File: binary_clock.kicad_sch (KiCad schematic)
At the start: 30 parts, among them P1 USB_C_Plug_USB2.0, SW1 RESET, SW2 BOOTSEL, U1 RP2040, U2 W25Q32JVSS, U3 AMS1117-3.3, Y1 Crystal_GND23

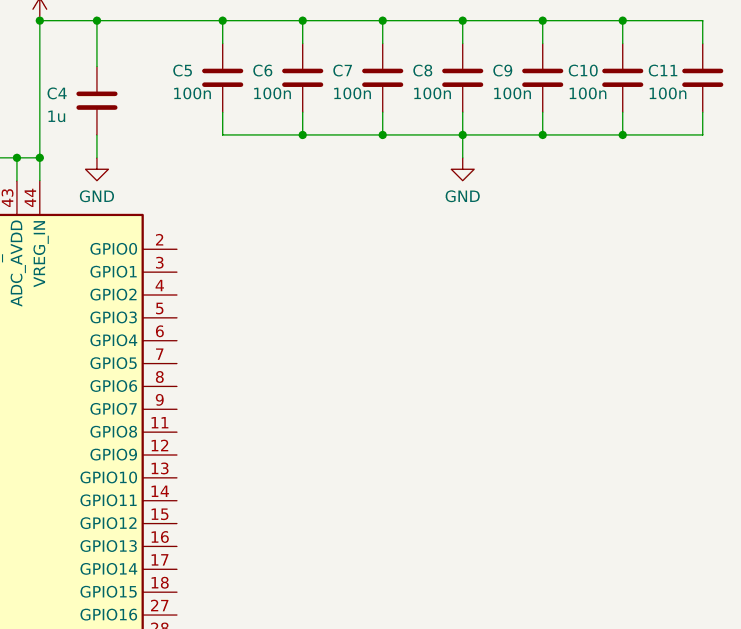
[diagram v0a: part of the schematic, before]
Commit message: added switches and labels for i2c0
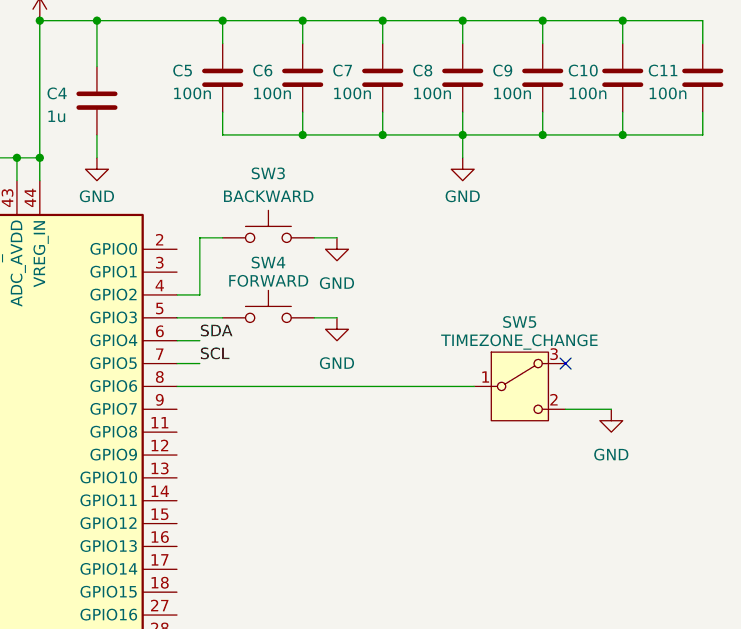
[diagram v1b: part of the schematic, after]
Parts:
- added SW3: BACKWARD, Button_Switch_SMD:SW_SPST_TS-1088-xR020, symbol Switch:SW_Push
- added SW4: FORWARD, Button_Switch_SMD:SW_SPST_TS-1088-xR020, symbol Switch:SW_Push
- added SW5: TIMEZONE_CHANGE, switch:SW_Slide_8.6x3.8x7.0_P2.54mm, symbol Switch:SW_Wuerth_450301014042
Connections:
- net GND: now also SW3.2, SW4.2, SW5.2 (C)
- net at U1.4 (GPIO2): now also SW3.1
- net at U1.5 (GPIO3): now also SW4.1
- net SDA: now reaches U1.6 (GPIO4)
- net SCL: now reaches U1.7 (GPIO5)
- net at U1.8 (GPIO6): now also SW5.1 (B)
- no-connect marks 7 -> 8

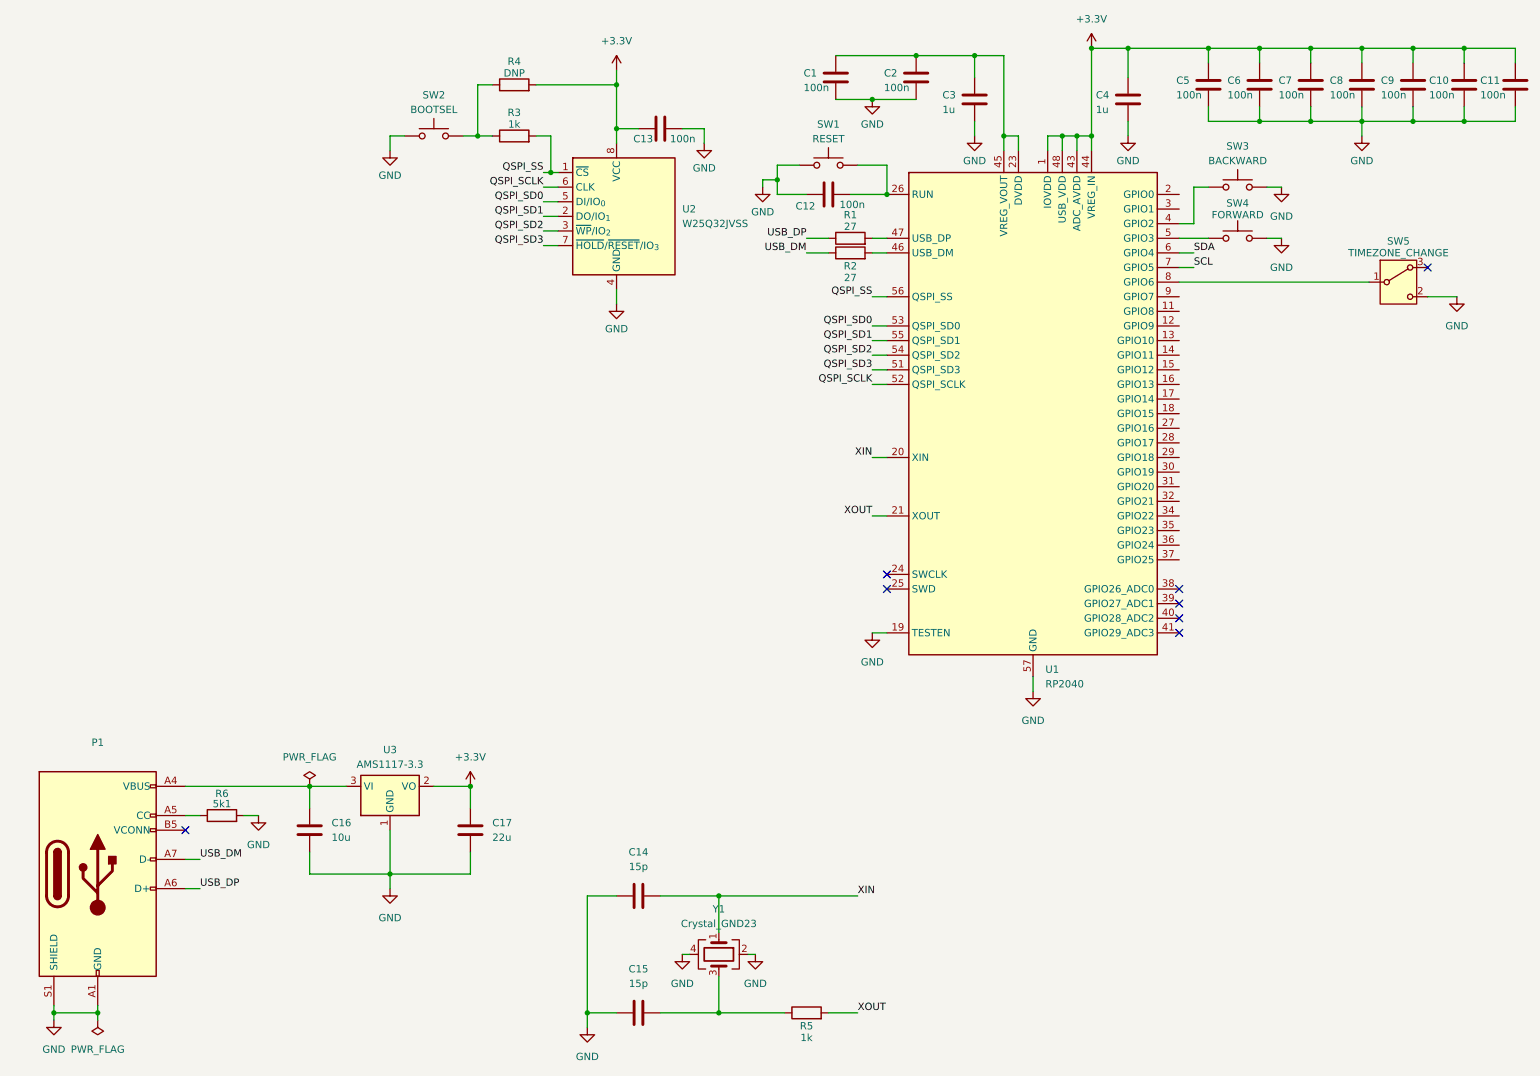
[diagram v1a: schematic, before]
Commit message: added rtc clock and diodes
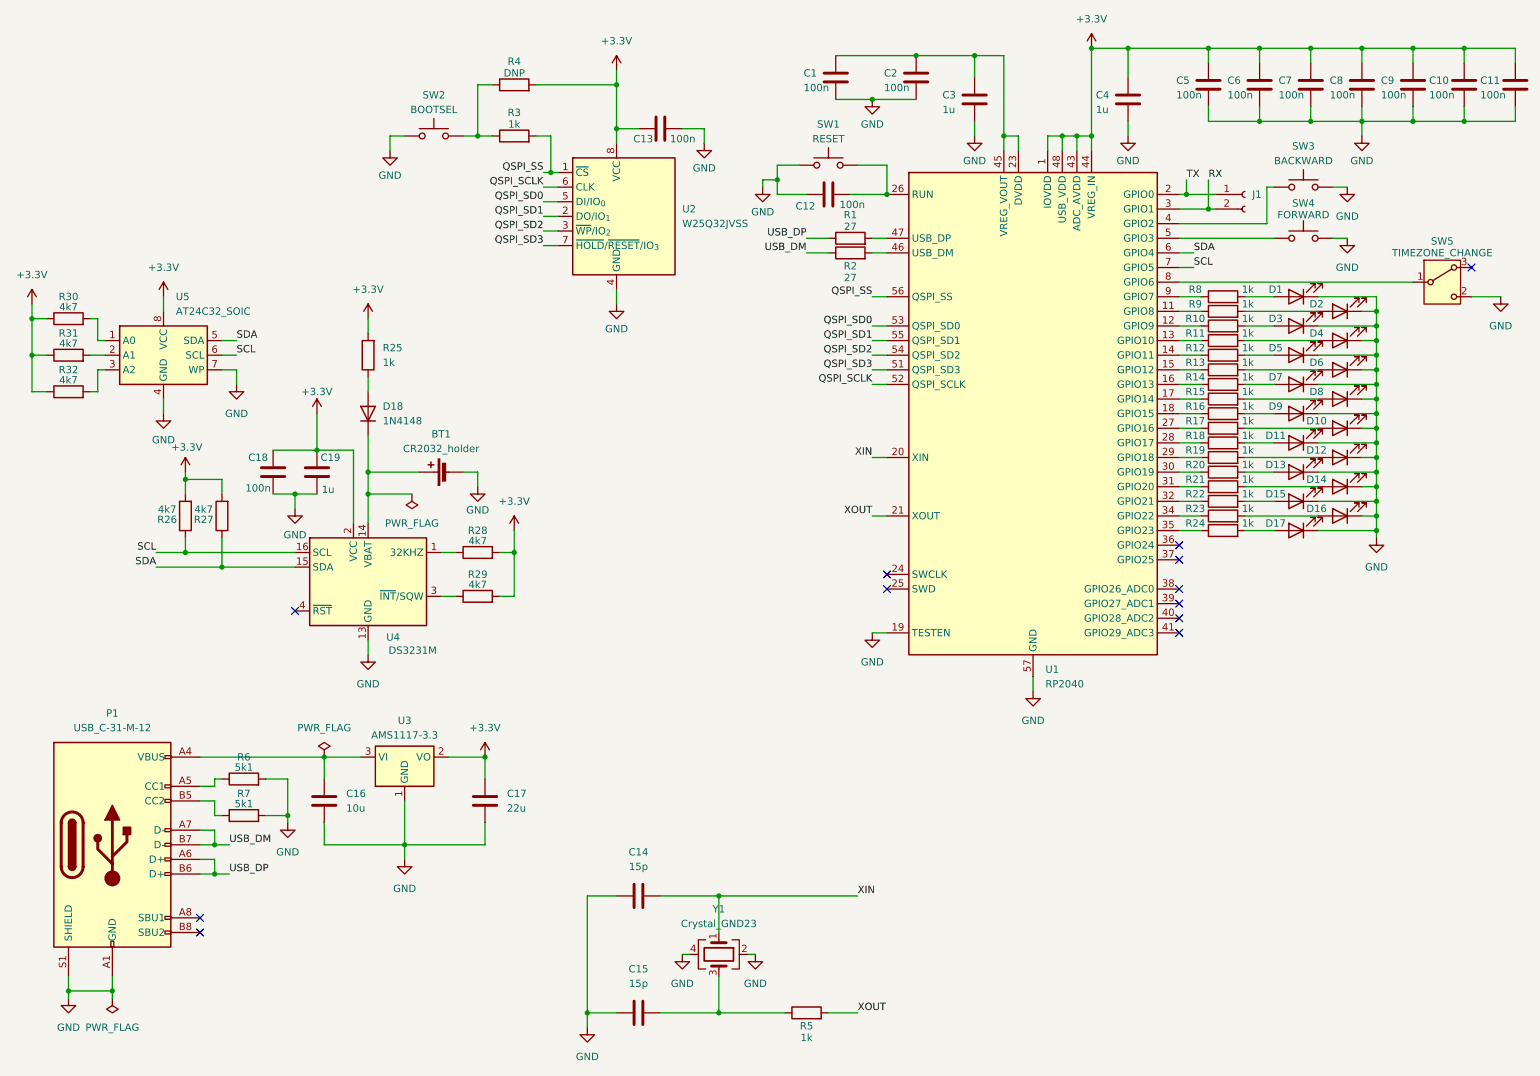
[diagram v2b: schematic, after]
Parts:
- removed P1: USB_C_Plug_USB2.0, Connector_USB:USB_C_Receptacle_GCT_USB4135-GF-A_6P_TopMnt_Horizontal, symbol Connector:USB_C_Plug_USB2.0
- added BT1: CR2032_holder, custom_footprints:Battery_Holder_Coin_2032_BS-7, symbol Device:Battery_Cell
- added C18: 100n, Capacitor_SMD:C_0603_1608Metric, symbol Device:C
- added C19: 1u, Capacitor_SMD:C_0603_1608Metric, symbol Device:C
- added D1, D10, D11, D12, D13, D14, D15, D16, D17, D2, D3, D4, D5, D6, D7, D8, D9: LED, LED_THT:LED_D3.0mm, symbol Device:LED
- added D18: 1N4148, Diode_THT:D_DO-35_SOD27_P7.62mm_Horizontal, symbol Diode:1N4148
- added J1: Conn_01x02_Socket, Connector_PinHeader_2.54mm:PinHeader_1x02_P2.54mm_Vertical, symbol Connector:Conn_01x02_Socket
- added P1: USB_C-31-M-12, Connector_USB:USB_C_Receptacle_HRO_TYPE-C-31-M-12, symbol Connector:USB_C_Receptacle_USB2.0_16P
- added R10, R11, R12, R13, R14, R15, R16, R17, R18, R19, R20, R21, R22, R23, R24, R8, R9: 1k, Resistor_SMD:R_0603_1608Metric, symbol Device:R
- added R25: 1k, Resistor_THT:R_Axial_DIN0207_L6.3mm_D2.5mm_P7.62mm_Horizontal, symbol Device:R
- added R26, R27, R28, R29, R30, R31, R32: 4k7, Resistor_SMD:R_0603_1608Metric, symbol Device:R
- added R7: 5k1, Resistor_SMD:R_0603_1608Metric, symbol Device:R
- added U4: DS3231M, Package_SO:SOIC-16W_7.5x10.3mm_P1.27mm, symbol Timer_RTC:DS3231M
- added U5: AT24C32_SOIC, Package_SO:SOIC-8_3.9x4.9mm_P1.27mm, symbol Memory_EEPROM:AT24CS32-SSHM
- SW5: footprint switch:SW_Slide_8.6x3.8x7.0_P2.54mm -> custom_footprints:SW_Slide_8.6x3.8x7.0_P2.54mm
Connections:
- net +3.3V: now also C18.2, C19.1, R25.2, R26.2, R27.2, R28.2, R29.2, R30.1, R31.1, R32.1, U4.2 (VCC), U5.8 (VCC)
- net GND: now also BT1.2 (-), C18.1, C19.2, D1.1 (K), D10.1 (K), D11.1 (K), D12.1 (K), D13.1 (K), D14.1 (K), D15.1 (K), D16.1 (K), D17.1 (K), D2.1 (K), D3.1 (K), D4.1 (K), D5.1 (K), D6.1 (K), D7.1 (K), D8.1 (K), D9.1 (K), P1.A1 (GND), P1.A12 (GND), P1.B1 (GND), P1.B12 (GND), P1.S1 (SHIELD), R7.2, U4.10 (GND), U4.11 (GND), U4.12 (GND), U4.13 (GND), U4.5 (GND), U4.6 (GND), U4.7 (GND), U4.8 (GND), U4.9 (GND), U5.4 (GND), U5.7 (WP)
- net SCL: now also R26.1, U4.16 (SCL), U5.6 (SCL)
- net SDA: now also R27.1, U4.15 (SDA), U5.5 (SDA)
- net USB_DM: now also P1.A7 (D-), P1.B7 (D-)
- net USB_DP: now also P1.A6 (D+), P1.B6 (D+)
- net at R6.1: now also P1.A5 (CC1)
- net at C16.2, U3.3 (VI): now also P1.A4 (VBUS), P1.A9 (VBUS), P1.B4 (VBUS), P1.B9 (VBUS)
- net at U1.11 (GPIO8): now also R9.1
- net at U1.12 (GPIO9): now also R10.1
- net at U1.13 (GPIO10): now also R11.1
- net at U1.14 (GPIO11): now also R12.1
- net at U1.15 (GPIO12): now also R13.1
- net at U1.16 (GPIO13): now also R14.1
- net at U1.17 (GPIO14): now also R15.1
- net at U1.18 (GPIO15): now also R16.1
- net TX: now reaches U1.2 (GPIO0)
- net TX: now also J1.1 (Pin_1)
- net at U1.27 (GPIO16): now also R17.1
- net at U1.28 (GPIO17): now also R18.1
- net at U1.29 (GPIO18): now also R19.1
- net RX: now reaches U1.3 (GPIO1)
- net RX: now also J1.2 (Pin_2)
- net at U1.30 (GPIO19): now also R20.1
- net at U1.31 (GPIO20): now also R21.1
- net at U1.32 (GPIO21): now also R22.1
- net at U1.34 (GPIO22): now also R23.1
- net at U1.35 (GPIO23): now also R24.1
- net at U1.9 (GPIO7): now also R8.1
- new net: D3.2 (A), R10.2
- new net: D9.2 (A), R16.2
- new net: R28.1, U4.1 (32KHZ)
- new net: BT1.1 (+), D18.1 (K), U4.14 (VBAT)
- new net: R29.1, U4.3 (~{INT}/SQW)
- new net: D18.2 (A), R25.1
- new net: D1.2 (A), R8.2
- new net: D15.2 (A), R22.2
- new net: D2.2 (A), R9.2
- new net: P1.B5 (CC2), R7.1
- new net: D6.2 (A), R13.2
- new net: D14.2 (A), R21.2
- new net: D12.2 (A), R19.2
- new net: D4.2 (A), R11.2
- new net: D17.2 (A), R24.2
- new net: D10.2 (A), R17.2
- new net: D5.2 (A), R12.2
- new net: D11.2 (A), R18.2
- new net: D7.2 (A), R14.2
- new net: D8.2 (A), R15.2
- new net: R31.2, U5.2 (A1)
- new net: R30.2, U5.1 (A0)
- new net: R32.2, U5.3 (A2)
- new net: D13.2 (A), R20.2
- new net: D16.2 (A), R23.2
- no-connect marks 8 -> 12
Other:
- moved on the sheet: C16, C17, SW3, SW4, SW5, U3

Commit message: final pcb, ignore production/
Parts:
- removed J1: Conn_01x02_Socket, Connector_PinHeader_2.54mm:PinHeader_1x02_P2.54mm_Vertical, symbol Connector:Conn_01x02_Socket
- added J1: Conn_01x03_Pin, Connector_PinHeader_2.54mm:PinHeader_1x03_P2.54mm_Vertical, symbol Connector:Conn_01x03_Pin
- P1: value USB_C-31-M-12 -> TYPE-C-31-M-12
- R1, R2: value 27 -> 33
- R4: now not fitted
- SW1: value RESET -> TS-1088-AR02016
- SW2: value BOOTSEL -> TS-1088-AR02016
- SW3: value BACKWARD -> TS-1088-AR02016
- SW4: value FORWARD -> TS-1088-AR02016
- Y1: value Crystal_GND23 -> ABM8-272-T3
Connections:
- net GND: now also J1.3 (Pin_3)
- net RX: now also J1.2 (Pin_2)
- net TX: now also J1.1 (Pin_1)
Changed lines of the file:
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@@
 	)
 	(junction
-		(at 224.79 46.99)
-		(diameter 0)
-		(color 0 0 0 0)
-	)
-	(junction
 		(at 125.73 35.56)
 		(diameter 0)
@@
 	)
 	(junction
-		(at 228.6 49.53)
-		(diameter 0)
-		(color 0 0 0 0)
-	)
-	(junction
 		(at 82.55 95.25)
 		(diameter 0)
@@
 	(wire
 		(pts
+			(xy 271.78 49.53) (xy 275.59 49.53)
+		)
+		(stroke
+			(width 0)
+			(type default)
+		)
+	)
+	(wire
+		(pts
 			(xy 257.81 67.31) (xy 255.27 67.31)
 		)
@@
 	(wire
 		(pts
-			(xy 238.76 45.72) (xy 238.76 52.07)
+			(xy 236.22 45.72) (xy 236.22 52.07)
 		)
 		(stroke
@@
 	(wire
 		(pts
-			(xy 223.52 49.53) (xy 228.6 49.53)
+			(xy 223.52 49.53) (xy 231.14 49.53)
 		)
 		(stroke
@@
 	(wire
 		(pts
+			(xy 271.78 44.45) (xy 275.59 44.45)
+		)
+		(stroke
+			(width 0)
+			(type default)
+		)
+	)
+	(wire
+		(pts
 			(xy 208.28 21.59) (xy 208.28 36.83)
 		)
@@
 	(wire
 		(pts
+			(xy 271.78 46.99) (xy 275.59 46.99)
+		)
+		(stroke
+			(width 0)
+			(type default)
+		)
+	)
+	(wire
+		(pts
 			(xy 281.94 24.13) (xy 281.94 21.59)
 		)
@@
 	(wire
 		(pts
-			(xy 238.76 45.72) (xy 240.03 45.72)
+			(xy 236.22 45.72) (xy 240.03 45.72)
 		)
 		(stroke
@@
 	(wire
 		(pts
-			(xy 223.52 46.99) (xy 224.79 46.99)
+			(xy 223.52 46.99) (xy 231.14 46.99)
 		)
 		(stroke
@@
 	(wire
 		(pts
-			(xy 228.6 49.53) (xy 229.87 49.53)
-		)
-		(stroke
-			(width 0)
-			(type default)
-		)
-	)
-	(wire
-		(pts
 			(xy 59.69 77.47) (xy 57.15 77.47)
 		)
@@
 	(wire
 		(pts
-			(xy 224.79 46.99) (xy 229.87 46.99)
-		)
-		(stroke
-			(width 0)
-			(type default)
-		)
-	)
-	(wire
-		(pts
 			(xy 46.99 64.77) (xy 46.99 67.31)
 		)
@@
 	(wire
 		(pts
-			(xy 228.6 44.45) (xy 228.6 49.53)
-		)
-		(stroke
-			(width 0)
-			(type default)
-		)
-	)
-	(wire
-		(pts
 			(xy 273.05 31.75) (xy 273.05 34.29)
 		)
@@
 	(wire
 		(pts
-			(xy 250.19 45.72) (xy 252.73 45.72)
+			(xy 250.19 45.72) (xy 257.81 45.72)
 		)
 		(stroke
@@
 	(wire
 		(pts
-			(xy 224.79 44.45) (xy 224.79 46.99)
-		)
-		(stroke
-			(width 0)
-			(type default)
-		)
-	)
-	(wire
-		(pts
 			(xy 255.27 102.87) (xy 257.81 102.87)
 		)
@@
 	(wire
 		(pts
-			(xy 223.52 52.07) (xy 238.76 52.07)
+			(xy 223.52 52.07) (xy 236.22 52.07)
 		)
 		(stroke
@@
 	)
 	(label "RX"
-		(at 228.6 44.45 0)
+		(at 231.14 49.53 0)
 		(effects
 			(font
@@
 		)
 	)
+	(label "RX"
+		(at 275.59 46.99 0)
+		(effects
+			(font
+				(size 1.27 1.27)
+			)
+			(justify left bottom)
+		)
+	)
 	(label "QSPI_SS"
 		(at 170.18 64.77 180)
@@
 		)
 	)
+	(label "TX"
+		(at 275.59 44.45 0)
+		(effects
+			(font
+				(size 1.27 1.27)
+			)
+			(justify left bottom)
+		)
+	)
 	(label "XOUT"
 		(at 167.64 189.23 0)
@@
 	)
 	(label "TX"
-		(at 224.79 44.45 0)
+		(at 231.14 46.99 0)
 		(effects
 			(font
@@
 			)
 		)
-		(property "Value" "27"
+		(property "Value" "33"
 			(at 166.37 52.578 90)
 			(effects
@@
 	)
 	(symbol
+		(lib_id "Connector:Conn_01x03_Pin")
+		(at 266.7 46.99 0)
+		(unit 1)
+		(exclude_from_sim no)
+		(in_bom yes)
+		(on_board yes)
+		(dnp no)
+		(fields_autoplaced yes)
+		(property "Reference" "J1"
+			(at 267.335 39.37 0)
+			(effects
+				(font
+					(size 1.27 1.27)
+				)
+			)
+		)
+		(property "Value" "Conn_01x03_Pin"
+			(at 267.335 41.91 0)
+			(effects
+				(font
+					(size 1.27 1.27)
+				)
+			)
+		)
+		(property "Footprint" "Connector_PinHeader_2.54mm:PinHeader_1x03_P2.54mm_Vertical"
+			(at 266.7 46.99 0)
+			(effects
+				(font
+					(size 1.27 1.27)
+				)
+				(hide yes)
+			)
+		)
+		(property "Datasheet" "~"
+			(at 266.7 46.99 0)
+			(effects
+				(font
+					(size 1.27 1.27)
+				)
+				(hide yes)
+			)
+		)
+		(property "Description" "Generic connector, single row, 01x03, script generated"
+			(at 266.7 46.99 0)
+			(effects
+				(font
+					(size 1.27 1.27)
+				)
+				(hide yes)
+			)
+		)
+		(pin "1"
+		)
+		(pin "3"
+		)
+		(pin "2"
+		)
+		(instances
+			(project "binary_clock"
+				(path "/e502a73f-a3d5-4755-8e23-06b2a601e58a"
+					(reference "J1")
+					(unit 1)
+				)
+			)
+		)
+	)
+	(symbol
 		(lib_id "power:GND")
 		(at 86.36 39.37 0)
@@
 		(in_bom yes)
 		(on_board yes)
-		(dnp no)
+		(dnp yes)
 		(property "Reference" "R4"
 			(at 107.95 23.876 90)
@@
 			)
 		)
-		(property "Value" "RESET"
+		(property "Value" "TS-1088-AR02016"
 			(at 162.56 37.338 0)
 			(effects
@@
 			)
 		)
-		(property "Value" "USB_C-31-M-12"
+		(property "Value" "TYPE-C-31-M-12"
 			(at 38.1 139.7 0)
 			(effects
@@
 	)
 	(symbol
-		(lib_id "Connector:Conn_01x02_Socket")
-		(at 234.95 46.99 0)
+		(lib_id "power:GND")
+		(at 275.59 49.53 0)
 		(unit 1)
 		(exclude_from_sim no)
@@
 		(on_board yes)
 		(dnp no)
-		(fields_autoplaced yes)
-		(property "Reference" "J1"
-			(at 236.22 46.9899 0)
+		(property "Reference" "#PWR035"
+			(at 275.59 55.88 0)
 			(effects
 				(font
 					(size 1.27 1.27)
 				)
-				(justify left)
+				(hide yes)
 			)
 		)
-		(property "Value" "Conn_01x02_Socket"
-			(at 236.22 49.5299 0)
+		(property "Value" "GND"
+			(at 275.59 53.848 0)
 			(effects
 				(font
 					(size 1.27 1.27)
 				)
-				(justify left)
-				(hide yes)
 			)
 		)
-		(property "Footprint" "Connector_PinHeader_2.54mm:PinHeader_1x02_P2.54mm_Vertical"
-			(at 234.95 46.99 0)
+		(property "Footprint" ""
+			(at 275.59 49.53 0)
 			(effects
 				(font
@@
 			)
 		)
-		(property "Datasheet" "~"
-			(at 234.95 46.99 0)
+		(property "Datasheet" ""
+			(at 275.59 49.53 0)
 			(effects
 				(font
@@
 			)
 		)
-		(property "Description" "Generic connector, single row, 01x02, script generated"
-			(at 234.95 46.99 0)
+		(property "Description" "Power symbol creates a global label with name \"GND\" , ground"
+			(at 275.59 49.53 0)
 			(effects
 				(font
@@
 			)
 		)
-		(pin "2"
-		)
 		(pin "1"
 		)
 		(instances
-			(project ""
+			(project "binary_clock"
 				(path "/e502a73f-a3d5-4755-8e23-06b2a601e58a"
-					(reference "J1")
+					(reference "#PWR035")
 					(unit 1)
 				)
@@
 			)
 		)
-		(property "Value" "BACKWARD"
-			(at 245.11 41.148 0)
+		(property "Value" "TS-1088-AR02016"
+			(at 243.586 41.148 0)
 			(effects
 				(font
@@
 			)
 		)
-		(property "Value" "FORWARD"
-			(at 245.11 50.546 0)
+		(property "Value" "TS-1088-AR02016"
+			(at 245.872 50.292 0)
 			(effects
 				(font
@@
 			)
 		)
-		(property "Value" "BOOTSEL"
+		(property "Value" "TS-1088-AR02016"
 			(at 93.98 32.258 0)
 			(effects
@@
 	(symbol
 		(lib_id "power:GND")
-		(at 252.73 45.72 0)
+		(at 257.81 45.72 0)
 		(unit 1)
 		(exclude_from_sim no)
@@
 		(fields_autoplaced yes)
 		(property "Reference" "#PWR022"
-			(at 252.73 52.07 0)
+			(at 257.81 52.07 0)
 			(effects
 				(font
@@
 		)
 		(property "Value" "GND"
-			(at 252.73 50.8 0)
+			(at 257.81 50.8 0)
 			(effects
 				(font
@@
 		)
 		(property "Footprint" ""
-			(at 252.73 45.72 0)
+			(at 257.81 45.72 0)
 			(effects
 				(font
@@
 		)
 		(property "Datasheet" ""
-			(at 252.73 45.72 0)
+			(at 257.81 45.72 0)
 			(effects
 				(font
@@
 		)
 		(property "Description" "Power symbol creates a global label with name \"GND\" , ground"
-			(at 252.73 45.72 0)
+			(at 257.81 45.72 0)
 			(effects
 				(font
@@
 			)
 		)
-		(property "Value" "27"
+		(property "Value" "33"
 			(at 166.37 61.468 90)
 			(effects
@@
 			)
 		)
-		(property "Value" "Crystal_GND23"
+		(property "Value" "ABM8-272-T3"
 			(at 143.51 173.736 90)
 			(effects
